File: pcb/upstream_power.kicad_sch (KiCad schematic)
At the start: 0 parts

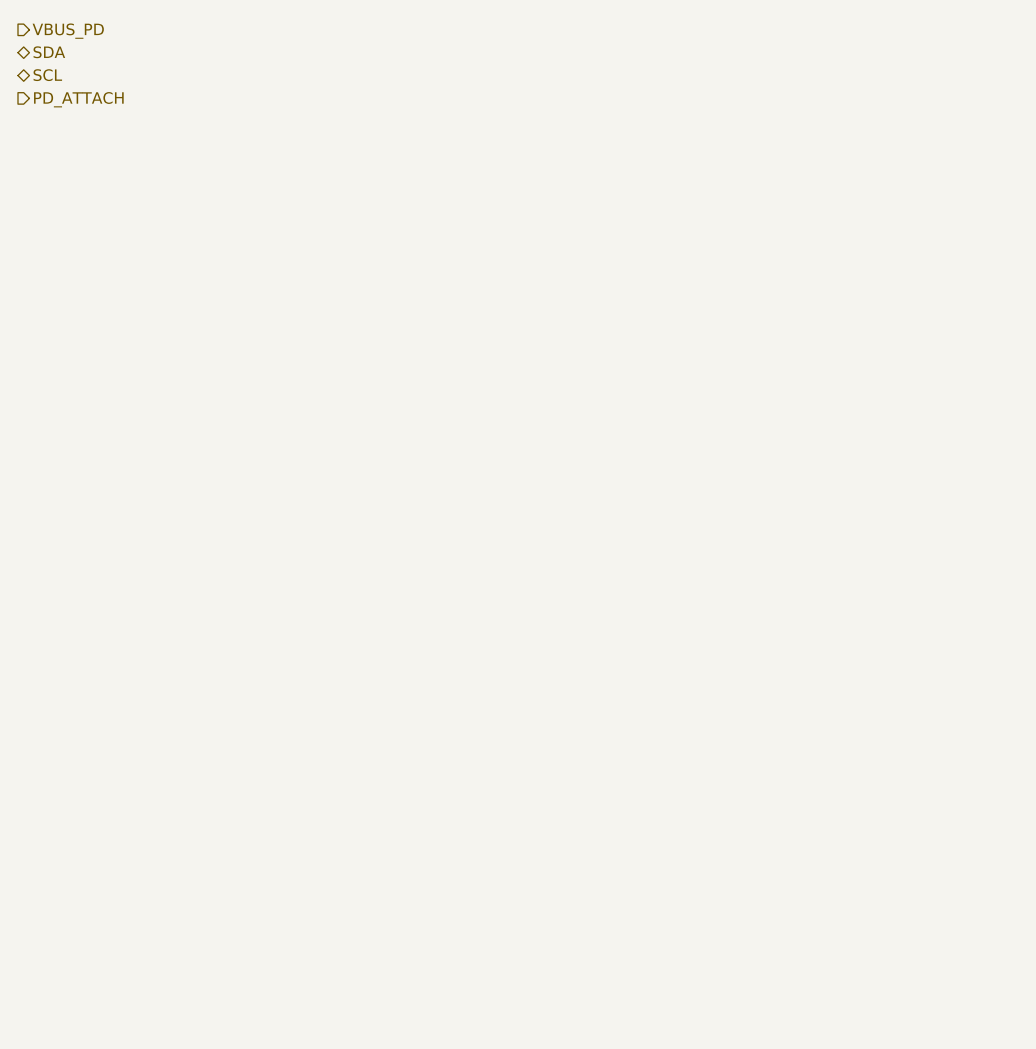
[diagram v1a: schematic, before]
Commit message: draw the power port, and move its switch to the part that can drive it
The receptacle, the sink that negotiates on it, and its supply capacitor. The
terminations are inside the sink, so the configuration pins go straight across.
The bus pull-ups are not repeated here -- they live once, beside the charger.

Drawing it settled the open question about isolating this connector, and not the
way the question was framed. The sink has no output switch to open; it drives an
external one. But the charger already brings out a charge-pump drive for a
back-to-back pair on its own input, raises their gates above their common source
when the input is valid, and does the reverse blocking itself. That is the same
arrangement, from a part already in the design, with the gate drive and the
input-valid detection solved rather than designed. So the switch belongs beside
the charger, this sheet exports raw connector voltage, and the sink's gate output
goes unused.

The hardware attach signal comes out with it. The sink has no attach output, and
a plain divider cannot span five to nine volts into a three-and-a-quarter volt
input -- the ratio needed to read high at five is the one that reads over the
limit at nine. It was redundant anyway: the charger reports a valid input over
the same bus, and the sink's driver already reports the contract. That frees the
pin it held.

Co-Authored-By: Claude Opus 5 (1M context) <noreply@anthropic.com>
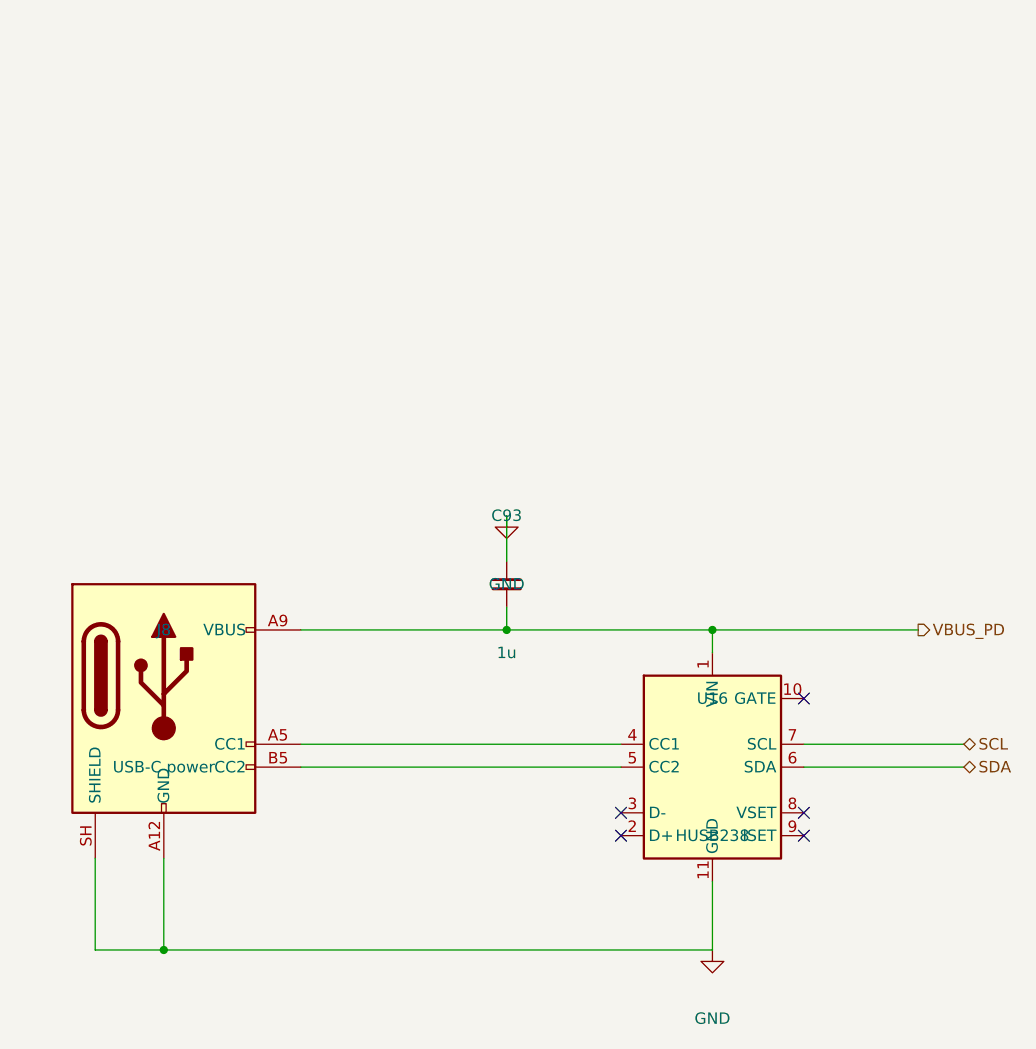
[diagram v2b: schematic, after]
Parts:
- added C93: 1u, symbol Device:C_Small
- added J8: USB-C power, symbol Connector:USB_C_Receptacle_PowerOnly_6P
- added U16: HUSB238, symbol Interface_USB:HUSB238_xxxDD
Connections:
- net SCL: now also U16.7 (SCL)
- net SDA: now also U16.6 (SDA)
- net VBUS_PD: now also C93.2, J8.A9 (VBUS), J8.B9 (VBUS), U16.1 (VIN)
- new net: J8.A5 (CC1), U16.4 (CC1)
- new net: J8.B5 (CC2), U16.5 (CC2)
- new net GND: C93.1, J8.A12 (GND), J8.B12 (GND), J8.SH (SHIELD), U16.11 (GND)
- no-connect marks 0 -> 5

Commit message: fit the sink's set resistors, which are the contract the board boots on
A fixed 100uA flows out of each of the sink's two set pins, so a resistor to ground states a
requested voltage and current as a plain analogue level, and the part asks for them on its own the
moment a charger is attached. That is not a hardware default sitting behind the bus interface, as
this document had it: the rail those resistors bring up is the one that powers the processor, so
with a flat cell there is no firmware awake to ask for anything. They are the only way the board
starts.

So they ask for the modest contract rather than the wanted one. They have to succeed against
whatever charger is on the end of the cable, and a cold boot draws a fraction of what a working
board does. 6.04k selects 9V, which anything calling itself a fast charger offers; 10.5k asks for
2A of it, and 18W is the smallest 9V offer in circulation, so an 18W, 20W, 30W or 65W charger all
satisfy it -- where asking for the full 3A the budget wants would only match the 27W-and-up part of
the field. The larger contract is then taken by the firmware, which selects a source capability by
index over the bus once it is running, on a path already proven on hardware. The request is the
lower of the resistor setting and the internal default, so these are a ceiling as well as a
request, which is the right way round for a bootstrap.

The open item they replace is the case the values are chosen to make rare rather than impossible:
a charger offering no 9V at all. The design already names 5V as an acceptable input with the ports
held to the battery budget, so the outcome is fine; what wants confirming is that the part reaches
it by itself rather than sitting with no contract.

The project's rule check is unchanged at the same known violations, and the two pins now read as
their own nets instead of the no-connects they were.

Co-Authored-By: Claude Opus 5 (1M context) <noreply@anthropic.com>
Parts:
- added R57: 6.04k, symbol Device:R_Small
- added R58: 10.5k, symbol Device:R_Small
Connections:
- net GND: now also R57.2, R58.2
- net at U16.8 (VSET): now also R57.1
- net at U16.9 (ISET): now also R58.1
- no-connect marks 5 -> 3
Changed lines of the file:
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@@
-	)
-	(no_connect
-		(at 147.32 127.00)
-	)
-	(no_connect
-		(at 147.32 129.54)
 	)
 	(no_connect
@@
 		)
 	)
+	(symbol
+		(lib_id "Device:R_Small")
+		(at 160.02 132.08 0)
+		(unit 1)
+		(exclude_from_sim no)
+		(in_bom yes)
+		(on_board yes)
+		(dnp no)
+		(property "Reference" "R57"
+			(at 160.02 124.46 0)
+			(effects
+				(font
+					(size 1.27 1.27)
+				)
+			)
+		)
+		(property "Value" "6.04k"
+			(at 160.02 139.70 0)
+			(effects
+				(font
+					(size 1.27 1.27)
+				)
+			)
+		)
+		(pin "1"
+		)		(pin "2"
+		)		(instances
+			(project "crossfire"
+				(path "/4c5cdd13-4f54-43b0-affb-0ae4b9a4d279/642c224c-a7f8-48f8-a755-d35ebfb11807"
+					(reference "R57")
+					(unit 1)
+				)			)
+		)
+	)
+	(symbol
+		(lib_id "Device:R_Small")
+		(at 152.40 132.08 0)
+		(unit 1)
+		(exclude_from_sim no)
+		(in_bom yes)
+		(on_board yes)
+		(dnp no)
+		(property "Reference" "R58"
+			(at 152.40 124.46 0)
+			(effects
+				(font
+					(size 1.27 1.27)
+				)
+			)
+		)
+		(property "Value" "10.5k"
+			(at 152.40 139.70 0)
+			(effects
+				(font
+					(size 1.27 1.27)
+				)
+			)
+		)
+		(pin "1"
+		)		(pin "2"
+		)		(instances
+			(project "crossfire"
+				(path "/4c5cdd13-4f54-43b0-affb-0ae4b9a4d279/642c224c-a7f8-48f8-a755-d35ebfb11807"
+					(reference "R58")
+					(unit 1)
+				)			)
+		)
+	)
+	(wire
+		(pts
+			(xy 147.32 127.00) (xy 160.02 127.00)
+		)
+		(stroke
+			(width 0)
+			(type solid)
+		)
+	)
+	(wire
+		(pts
+			(xy 160.02 127.00) (xy 160.02 129.54)
+		)
+		(stroke
+			(width 0)
+			(type solid)
+		)
+	)
+	(wire
+		(pts
+			(xy 147.32 129.54) (xy 152.40 129.54)
+		)
+		(stroke
+			(width 0)
+			(type solid)
+		)
+	)
 	(wire
 		(pts
@@
 	(wire
 		(pts
-			(xy 68.58 142.24) (xy 137.16 142.24)
+			(xy 68.58 142.24) (xy 160.02 142.24)
 		)
 		(stroke
@@
 	(symbol
 		(lib_id "power:GND")
-		(at 137.16 142.24 0)
+		(at 160.02 142.24 0)
 		(unit 1)
 		(exclude_from_sim no)
@@
 		(dnp no)
 		(property "Reference" "#PWR01"
-			(at 137.16 134.62 0)
+			(at 160.02 134.62 0)
 			(hide yes)
 			(effects
@@
 		)
 		(property "Value" "GND"
-			(at 137.16 149.86 0)
+			(at 160.02 149.86 0)
 			(effects
 				(font
@@
 		)
 		(stroke
+			(width 0)
+			(type solid)
+		)
+	)
+	(junction
+		(at 137.16 142.24)
+		(diameter 0)
+		(color 0 0 0 0)
+	)
+	(wire
+		(pts
+			(xy 152.40 134.62) (xy 152.40 142.24)
+		)
+		(stroke
+			(width 0)
+			(type solid)
+		)
+	)
+	(junction
+		(at 152.40 142.24)
+		(diameter 0)
+		(color 0 0 0 0)
+	)
+	(wire
+		(pts
+			(xy 160.02 134.62) (xy 160.02 142.24)
+		)
+		(stroke
